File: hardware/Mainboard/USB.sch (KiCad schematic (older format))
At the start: 9 parts, among them IC9 FT232RL, X2 SERIAL

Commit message: Misc: 	- Update README 	- Add 74HC138 datasheet 	- Update board image 	- Add layout for website tutorial
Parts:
- renumbered C14 to C10, C15 to C11, C16 to C12, D12 to D10, D11 to D9, IC9 to IC10, R6 to R7, R7 to R8, X2 to X5
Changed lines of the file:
@@
 $Descr A4 11693 8268
 encoding utf-8
-Sheet 7 7
+Sheet 6 7
 Title "Mainboard"
 Date "2020-01-17"
@@
 P 5650 3850
 AR Path="/5E95D1D6" Ref="IC?"  Part="1"
-AR Path="/5E9064F2/5E95D1D6" Ref="IC9"  Part="1"
-F 0 "IC9" H 5050 4750 50  0000 C CNN
+AR Path="/5E9064F2/5E95D1D6" Ref="IC10"  Part="1"
+F 0 "IC10" H 5050 4750 50  0000 C CNN
 F 1 "FT232RL" H 5150 2950 50  0000 C CNN
 F 2 "Package_SO:SSOP-28_5.3x10.2mm_P0.65mm" H 5650 3850 50  0001 C CNN
@@
 P 7675 3950
 AR Path="/5E95D1F2" Ref="R?"  Part="1"
-AR Path="/5E9064F2/5E95D1F2" Ref="R7"  Part="1"
-F 0 "R7" H 7745 3996 50  0000 L CNN
-F 1 "1k" H 7745 3905 50  0000 L CNN
+AR Path="/5E9064F2/5E95D1F2" Ref="R8"  Part="1"
+F 0 "R8" V 7675 3900 50  0000 L CNN
+F 1 "1k" V 7750 3900 50  0000 L CNN
 F 2 "Resistor_SMD:R_0805_2012Metric" V 7605 3950 50  0001 C CNN
 F 3 "https://www.mouser.de/datasheet/2/447/Yageo%20LR_MFP_2013-594635.pdf" H 7675 3950 50  0001 C CNN
@@
 P 7675 3500
 AR Path="/5E95D1F8" Ref="D?"  Part="1"
-AR Path="/5E9064F2/5E95D1F8" Ref="D12"  Part="1"
-F 0 "D12" V 7714 3382 50  0000 R CNN
+AR Path="/5E9064F2/5E95D1F8" Ref="D10"  Part="1"
+F 0 "D10" V 7714 3382 50  0000 R CNN
 F 1 "RX" V 7623 3382 50  0000 R CNN
 F 2 "LED_SMD:LED_0805_2012Metric" H 7675 3500 50  0001 C CNN
@@
 P 4650 3150
 AR Path="/5E95D20C" Ref="C?"  Part="1"
-AR Path="/5E9064F2/5E95D20C" Ref="C14"  Part="1"
-F 0 "C14" H 4765 3196 50  0000 L CNN
+AR Path="/5E9064F2/5E95D20C" Ref="C10"  Part="1"
+F 0 "C10" H 4765 3196 50  0000 L CNN
 F 1 "100nF" H 4765 3105 50  0000 L CNN
 F 2 "Capacitor_SMD:C_0805_2012Metric" H 4688 3000 50  0001 C CNN
@@
 P 4500 3150
 AR Path="/5E95D212" Ref="#PWR?"  Part="1"
-AR Path="/5E9064F2/5E95D212" Ref="#PWR049"  Part="1"
-F 0 "#PWR049" H 4500 2900 50  0001 C CNN
+AR Path="/5E9064F2/5E95D212" Ref="#PWR062"  Part="1"
+F 0 "#PWR062" H 4500 2900 50  0001 C CNN
 F 1 "GND" H 4505 2977 50  0000 C CNN
 F 2 "" H 4500 3150 50  0001 C CNN
@@
 P 7600 3250
 AR Path="/5E95D229" Ref="#PWR?"  Part="1"
-AR Path="/5E9064F2/5E95D229" Ref="#PWR055"  Part="1"
-F 0 "#PWR055" H 7600 3100 50  0001 C CNN
+AR Path="/5E9064F2/5E95D229" Ref="#PWR068"  Part="1"
+F 0 "#PWR068" H 7600 3100 50  0001 C CNN
 F 1 "+5V" H 7615 3423 50  0000 C CNN
 F 2 "" H 7600 3250 50  0001 C CNN
@@
 P 3150 3950
 AR Path="/5E95D244" Ref="#PWR?"  Part="1"
-AR Path="/5E9064F2/5E95D244" Ref="#PWR047"  Part="1"
-F 0 "#PWR047" H 3150 3700 50  0001 C CNN
+AR Path="/5E9064F2/5E95D244" Ref="#PWR061"  Part="1"
+F 0 "#PWR061" H 3150 3700 50  0001 C CNN
 F 1 "GND" H 3155 3777 50  0000 C CNN
 F 2 "" H 3150 3950 50  0001 C CNN
@@
 P 5550 2000
 AR Path="/5ECF03CA" Ref="#PWR?"  Part="1"
-AR Path="/5E9064F2/5ECF03CA" Ref="#PWR051"  Part="1"
-F 0 "#PWR051" H 5550 1850 50  0001 C CNN
+AR Path="/5E9064F2/5ECF03CA" Ref="#PWR064"  Part="1"
+F 0 "#PWR064" H 5550 1850 50  0001 C CNN
 F 1 "+5V" H 5565 2173 50  0000 C CNN
 F 2 "" H 5550 2000 50  0001 C CNN
@@
 P 5650 5050
 AR Path="/5ECF08BF" Ref="#PWR?"  Part="1"
-AR Path="/5E9064F2/5ECF08BF" Ref="#PWR052"  Part="1"
-F 0 "#PWR052" H 5650 4800 50  0001 C CNN
+AR Path="/5E9064F2/5ECF08BF" Ref="#PWR065"  Part="1"
+F 0 "#PWR065" H 5650 4800 50  0001 C CNN
 F 1 "GND" H 5655 4877 50  0000 C CNN
 F 2 "" H 5650 5050 50  0001 C CNN
@@
 P 5400 2400
 AR Path="/5E2B4DFA" Ref="C?"  Part="1"
-AR Path="/5E9064F2/5E2B4DFA" Ref="C15"  Part="1"
-F 0 "C15" H 5515 2446 50  0000 L CNN
+AR Path="/5E9064F2/5E2B4DFA" Ref="C11"  Part="1"
+F 0 "C11" H 5515 2446 50  0000 L CNN
 F 1 "100nF" H 5515 2355 50  0000 L CNN
 F 2 "Capacitor_SMD:C_0805_2012Metric" H 5438 2250 50  0001 C CNN
@@
 P 5400 2650
 AR Path="/5E2B8CA7" Ref="#PWR?"  Part="1"
-AR Path="/5E9064F2/5E2B8CA7" Ref="#PWR050"  Part="1"
-F 0 "#PWR050" H 5400 2400 50  0001 C CNN
+AR Path="/5E9064F2/5E2B8CA7" Ref="#PWR063"  Part="1"
+F 0 "#PWR063" H 5400 2400 50  0001 C CNN
 F 1 "GND" H 5405 2477 50  0000 C CNN
 F 2 "" H 5400 2650 50  0001 C CNN
@@
 P 5900 2400
 AR Path="/5E2BDF0E" Ref="C?"  Part="1"
-AR Path="/5E9064F2/5E2BDF0E" Ref="C16"  Part="1"
-F 0 "C16" H 6015 2446 50  0000 L CNN
+AR Path="/5E9064F2/5E2BDF0E" Ref="C12"  Part="1"
+F 0 "C12" H 6015 2446 50  0000 L CNN
 F 1 "100nF" H 6015 2355 50  0000 L CNN
 F 2 "Capacitor_SMD:C_0805_2012Metric" H 5938 2250 50  0001 C CNN
@@
 P 5900 2650
 AR Path="/5E2BDF14" Ref="#PWR?"  Part="1"
-AR Path="/5E9064F2/5E2BDF14" Ref="#PWR054"  Part="1"
-F 0 "#PWR054" H 5900 2400 50  0001 C CNN
+AR Path="/5E9064F2/5E2BDF14" Ref="#PWR067"  Part="1"
+F 0 "#PWR067" H 5900 2400 50  0001 C CNN
 F 1 "GND" H 5905 2477 50  0000 C CNN
 F 2 "" H 5900 2650 50  0001 C CNN
@@
 P 5750 2000
 AR Path="/5D9D8F30" Ref="#PWR?"  Part="1"
-AR Path="/5E9064F2/5D9D8F30" Ref="#PWR053"  Part="1"
-F 0 "#PWR053" H 5750 1850 50  0001 C CNN
+AR Path="/5E9064F2/5D9D8F30" Ref="#PWR066"  Part="1"
+F 0 "#PWR066" H 5750 1850 50  0001 C CNN
 F 1 "+5V" H 5765 2173 50  0000 C CNN
 F 2 "" H 5750 2000 50  0001 C CNN
@@
 	7675 3350 7675 3300
 $Comp
-L Connector_Custom:USB-B X2
+L Connector_Custom:USB-B X?
 U 1 1 5DA7E5BF
 P 3200 3450
-AR Path="/5DA7E5BF" Ref="X2"  Part="1"
-AR Path="/5E9064F2/5DA7E5BF" Ref="X2"  Part="1"
-F 0 "X2" H 3257 3917 50  0000 C CNN
+AR Path="/5DA7E5BF" Ref="X?"  Part="1"
+AR Path="/5E9064F2/5DA7E5BF" Ref="X5"  Part="1"
+F 0 "X5" H 3257 3917 50  0000 C CNN
 F 1 "SERIAL" H 3257 3826 50  0000 C CNN
 F 2 "Connector_Custom:USB-B_TE_2923042_Horizontal" H 3350 3400 50  0001 C CNN
@@
 P 7525 3950
 AR Path="/5E95D1EC" Ref="R?"  Part="1"
-AR Path="/5E9064F2/5E95D1EC" Ref="R6"  Part="1"
-F 0 "R6" H 7595 3996 50  0000 L CNN
-F 1 "1k" H 7595 3905 50  0000 L CNN
+AR Path="/5E9064F2/5E95D1EC" Ref="R7"  Part="1"
+F 0 "R7" V 7525 3900 50  0000 L CNN
+F 1 "1k" V 7600 3900 50  0000 L CNN
 F 2 "Resistor_SMD:R_0805_2012Metric" V 7455 3950 50  0001 C CNN
 F 3 "https://www.mouser.de/datasheet/2/447/Yageo%20LR_MFP_2013-594635.pdf" H 7525 3950 50  0001 C CNN
@@
 P 7525 3500
 AR Path="/5E95D1E6" Ref="D?"  Part="1"
-AR Path="/5E9064F2/5E95D1E6" Ref="D11"  Part="1"
-F 0 "D11" V 7564 3382 50  0000 R CNN
+AR Path="/5E9064F2/5E95D1E6" Ref="D9"  Part="1"
+F 0 "D9" V 7564 3382 50  0000 R CNN
 F 1 "TX" V 7473 3382 50  0000 R CNN
 F 2 "LED_SMD:LED_0805_2012Metric" H 7525 3500 50  0001 C CNN

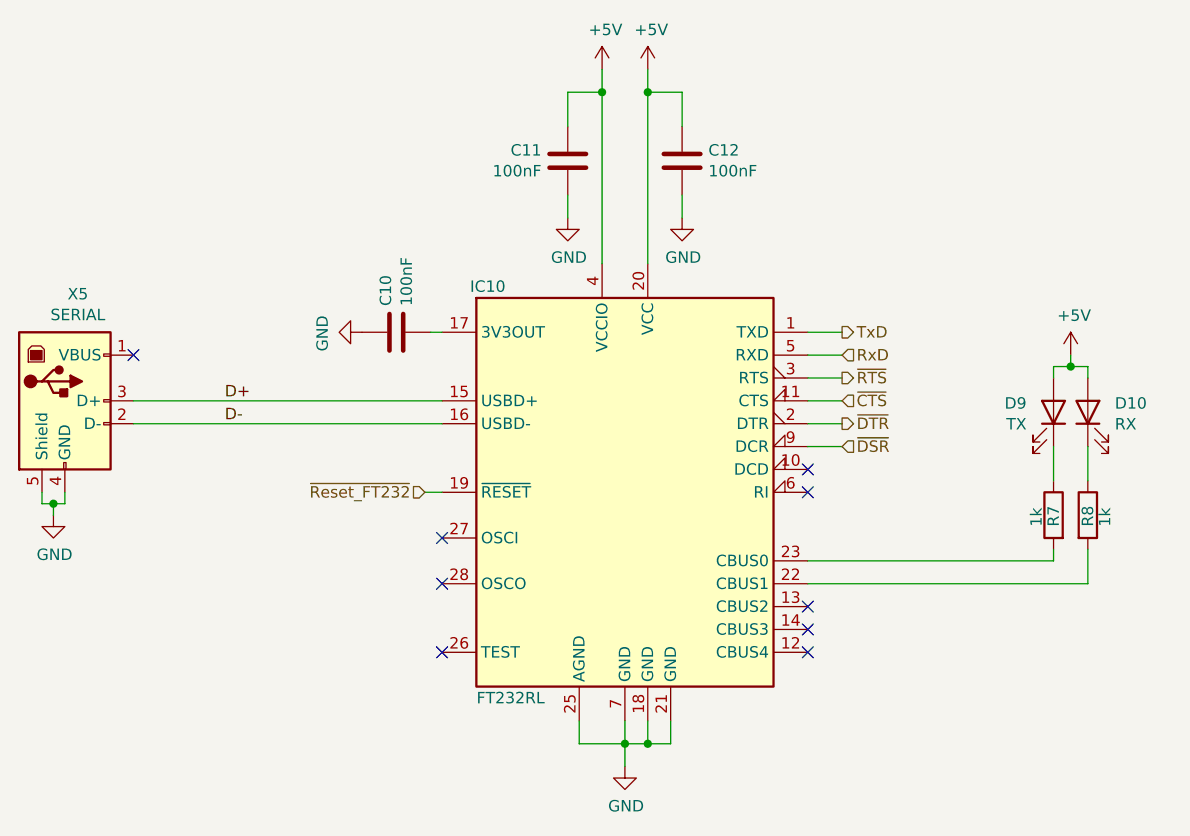
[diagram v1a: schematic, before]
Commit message: Hardware: 	- Add pull up resistor for PB
Documentation:
	- Add more datasheets
	- Update documentation

Misc:
	- Rename CHANGELOG
	- Remove old files

Signed-off-by: Daniel Kampert <DanielKampert@kampis-elektroecke.de>
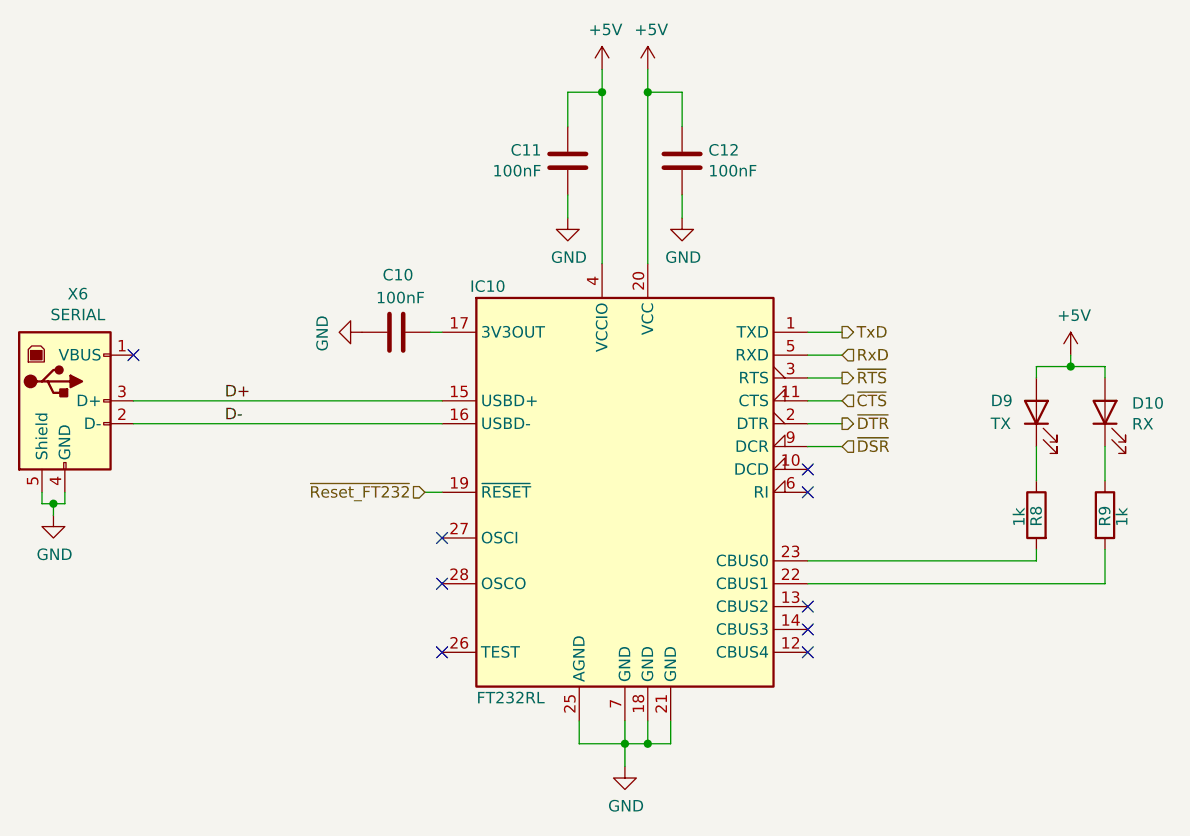
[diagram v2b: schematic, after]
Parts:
- C10, C11, C12: Distributor (none) -> Mouser; Order Number (none) -> 80-C0805C104K5R
- D10: Distributor (none) -> Mouser; Order Number (none) -> 604-APT2012PGW
- D9: Distributor (none) -> Mouser; Order Number (none) -> 604-APT2012PYW
- IC10: Distributor (none) -> Mouser; Order Number (none) -> 895-FT232RL
- R8: renamed from R7; Distributor (none) -> Mouser; Order Number (none) -> 603-MFP-25BRD52-1K
- R9: renamed from R8; Distributor (none) -> Mouser; Order Number (none) -> 603-MFP-25BRD52-1K
- X6: renamed from X5; Distributor (none) -> Mouser; Order Number (none) -> 571-292304-2
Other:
- moved on the sheet: D10, D9, R8, R9
